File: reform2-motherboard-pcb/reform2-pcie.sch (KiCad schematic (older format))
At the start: 51 parts, among them J10 1-2199230-6, J11 48099-5701, U11 679105700, U20 AP22815, U23 IDT5V41066, Y3 25MHz

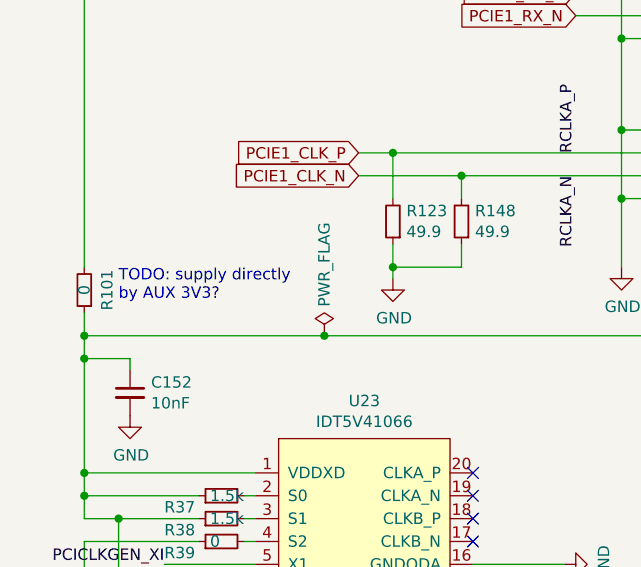
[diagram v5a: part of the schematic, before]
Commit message: reform2-motherboard: add pdf schematics
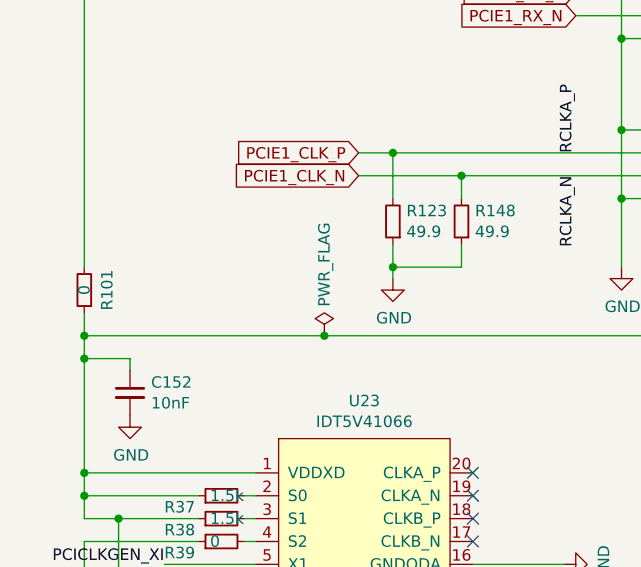
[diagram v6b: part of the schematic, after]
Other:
- note removed: "TODO: supply directly \nby AUX 3V3?"
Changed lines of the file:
@@
 Wire Wire Line
 	700  4900 700  5000
-Text Notes 850  4850 0    50   ~ 0
-TODO: supply directly \nby AUX 3V3?
 $Comp
 L power:PWR_FLAG #FLG0114
